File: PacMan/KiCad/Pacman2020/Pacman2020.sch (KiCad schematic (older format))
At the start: 13 parts, among them J10 Conn_01x02, J11 Conn_01x02, J12 Conn_01x02, J13 Conn_01x08, J5 Conn_01x04, J9 Conn_01x02, Q2 Q_NMOS_GDS

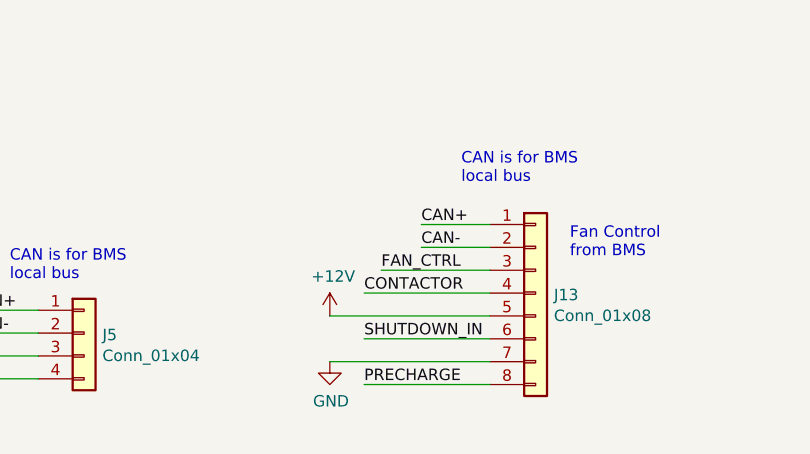
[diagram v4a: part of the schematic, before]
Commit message: update schematic and layout
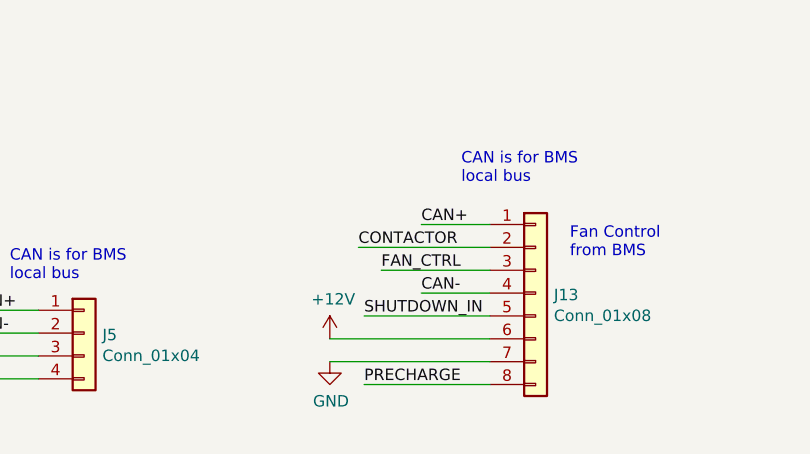
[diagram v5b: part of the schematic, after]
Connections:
- net +12V: now also J13.6 (Pin_6); no longer J13.5 (Pin_5)
- net CAN-: now also J13.4 (Pin_4); no longer J13.2 (Pin_2)
- net CONTACTOR: now also J13.2 (Pin_2); no longer J13.4 (Pin_4)
- net SHUTDOWN_IN: now also J13.5 (Pin_5); no longer J13.6 (Pin_6)
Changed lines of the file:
@@
 Wire Wire Line
 	5775 6775 6075 6775
-Text Label 5775 6875 0    50   ~ 0
+Text Label 5775 7075 0    50   ~ 0
 CAN-
 Wire Wire Line
-	5775 6875 6075 6875
+	5500 6875 6075 6875
 $Comp
 L power:GND #PWR0105
@@
 Wire Wire Line
 	5525 7475 6075 7475
-Text Label 5525 7075 0    50   ~ 0
+Text Label 5500 6875 0    50   ~ 0
 CONTACTOR
 Wire Wire Line
-	5525 7075 6075 7075
-Text Label 5525 7275 0    50   ~ 0
-SHUTDOWN_IN
-Wire Wire Line
-	5525 7275 6075 7275
+	5775 7075 6075 7075
 Text Label 1875 4775 0    50   ~ 0
 PRECHARGE
@@
 	10200 2825 10400 2825
 Wire Wire Line
-	5375 7375 6075 7375
-Wire Wire Line
 	6075 6975 5600 6975
 Text Label 5600 6975 0    50   ~ 0
@@
 L power:+12V #PWR0106
 U 1 1 6037F25F
-P 5375 7175
-F 0 "#PWR0106" H 5375 7025 50  0001 C CNN
-F 1 "+12V" H 5390 7348 50  0000 C CNN
-F 2 "" H 5375 7175 50  0001 C CNN
-F 3 "" H 5375 7175 50  0001 C CNN
-	1    5375 7175
-	1    0    0    -1
-$EndComp
-Wire Wire Line
-	5375 7175 6075 7175
+P 5375 7275
+F 0 "#PWR0106" H 5375 7125 50  0001 C CNN
+F 1 "+12V" H 5390 7448 50  0000 C CNN
+F 2 "" H 5375 7275 50  0001 C CNN
+F 3 "" H 5375 7275 50  0001 C CNN
+	1    5375 7275
+	1    0    0    -1
+$EndComp
+Wire Wire Line
+	5525 7175 6075 7175
 $Comp
 L Connector_Generic:Conn_01x04 J5
@@
 $EndComp
 Connection ~ 8450 3625
+Text Label 5525 7175 0    50   ~ 0
+SHUTDOWN_IN
+Wire Wire Line
+	5375 7275 6075 7275
+Wire Wire Line
+	5375 7375 6075 7375
 $EndSCHEMATC
